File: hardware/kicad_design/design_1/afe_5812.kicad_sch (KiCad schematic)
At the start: 62 parts, among them J10 Conn_Coaxial, J11 Conn_Coaxial, J12 Conn_Coaxial, J13 Conn_Coaxial, J5 Conn_Coaxial, J6 Conn_Coaxial, J8 Conn_Coaxial, J9 Conn_Coaxial, U4 AFE5812ZCF, X1 XO32

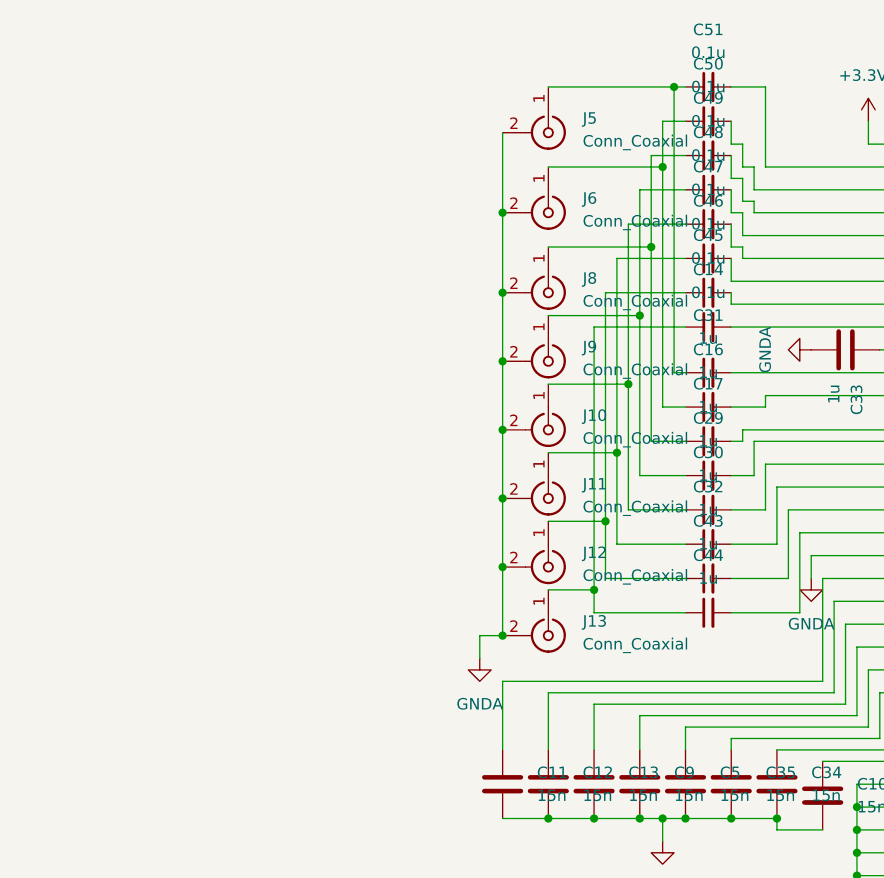
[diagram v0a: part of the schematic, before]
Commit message: rev 5 board with termination resistors, through hole usb c, and minor fixes
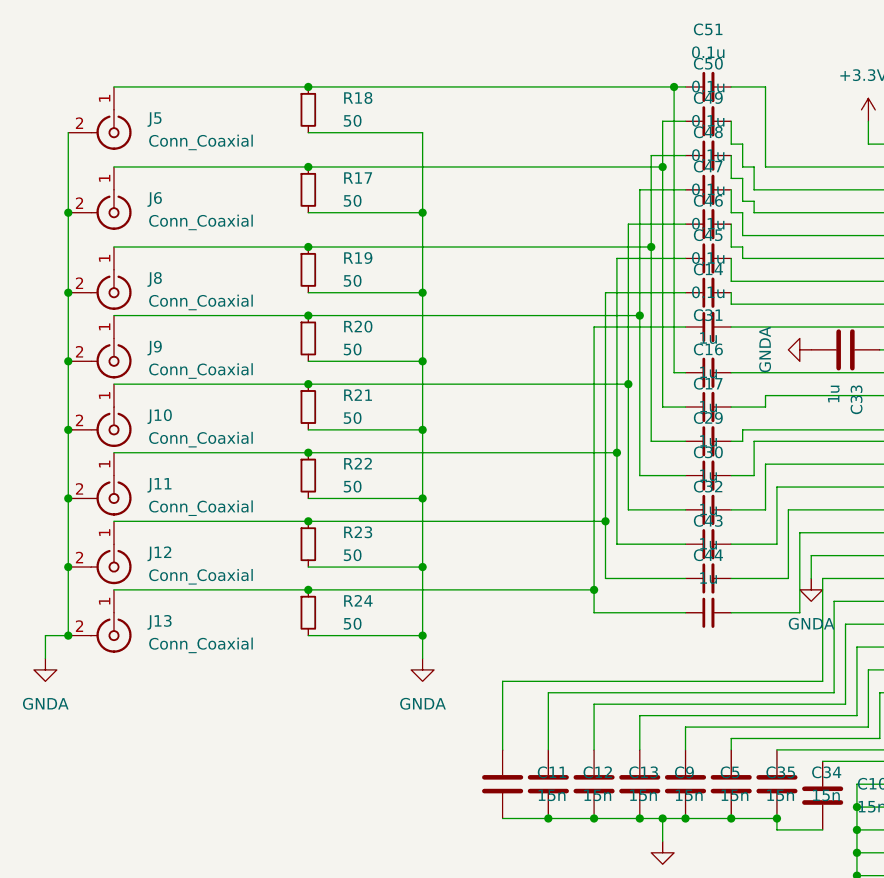
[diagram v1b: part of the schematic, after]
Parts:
- added R17, R18, R19, R20, R21, R22, R23, R24: 50, Resistor_SMD:R_0402_1005Metric, symbol Device:R_Small
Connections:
- net GNDA: now also R17.2, R18.2, R19.2, R20.2, R21.2, R22.2, R23.2, R24.2
- net at C14.1, C44.1, J13.1 (In): now also R24.1
- net at C17.1, C49.1, J8.1 (In): now also R19.1
- net at C29.1, C48.1, J9.1 (In): now also R20.1
- net at C30.1, C47.1, J10.1 (In): now also R21.1
- net at C32.1, C46.1, J11.1 (In): now also R22.1
- net at C43.1, C45.1, J12.1 (In): now also R23.1
- net at C31.1, C51.1, J5.1 (In): now also R18.1
- net at C16.1, C50.1, J6.1 (In): now also R17.1
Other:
- moved on the sheet: J10, J11, J12, J13, J5, J6, J8, J9
